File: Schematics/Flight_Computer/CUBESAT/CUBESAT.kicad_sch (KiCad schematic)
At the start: 44 parts, among them J1 6 Pin Connector, J2 M22-6003005, J3 U.FL-R-SMT_01_, U1 ADXL345BCCZ, U2 NEO-M8N-0, U3 IAM-20380, U4 MAGNETOMETER, U5 STM32F446RET6, U6 LM75AIM_NOPB

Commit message: feat: cleaned up schematic for FC
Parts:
- removed J1: 6 Pin Connector, CUBESAT:6 Pin Connector, symbol CUBESAT:6 Pin Connector
- removed R10, R9: 4.7k, CUBESAT:Resistor4.7kO, symbol CUBESAT:Resistor4.7kO
- removed R7: 100, CUBESAT:Reistor100O, symbol CUBESAT:Resistor100O
- added J1: Conn_01x06_Pin, CUBESAT:6 Pin Connector, symbol Connector:Conn_01x06_Pin
- added R11: 100, CUBESAT:Reistor100O, symbol Device:R
- added R13, R7: 4.7k, CUBESAT:Resistor4.7kO, symbol Device:R
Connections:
- net 3.3 V: now also J1.5 (Pin_5), J1.6 (Pin_6), R13.1, R7.1; no longer S2.4
- net I2C 3 SCL: now also R7.2
- net I2C 3 SDA: now also R13.2
- net NRST: now also J1.4 (Pin_4), R11.2
- net SWCLK: now also J1.2 (Pin_2)
- net SWDIO: now also J1.3 (Pin_3)
- net SWO: now also J1.1 (Pin_1)
- net at S1.1: now also R11.1
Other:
- moved on the sheet: C11, R8

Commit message: feat: new updated sch for better readibility
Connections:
- net 3.3 V: now also C14.1, C15.1, C16.1, C17.1, C8.1, R5.1; no longer C1.2, C10.1, C12.2, C13.2, C14.2, C15.2, C16.2, C17.2, C18.2, C19.2, C2.1, C21.2, C3.1, C4.1, C5.1, C6.2, C7.2, C8.2, C9.2, J1.6 (Pin_6), J2.2, J3.1 (GND), J3.2 (GND), R1.1, R4.2, R5.2, R6.2, R8.1, S1.2, S1.4, U1.2 (GND), U1.4 (GND), U1.5 (GND), U2.10 (GND), U2.12 (GND), U2.13 (GND), U2.24 (GND), U2.7 (VDD_USB), U3.10 (RESV9_1215), U3.11 (RESV9_1215), U3.12 (RESV9_1215), U3.13 (GND), U3.15 (RESV9_1215), U3.7 (RESV7), U3.9 (RESV9_1215), U4.3 (GND), U5.12 (VSSA/VREF-), U5.18 (VSS), U5.31 (VSS), U5.47 (VSS), U5.63 (VSS), U6.4 (GND), U6.5 (A2), U6.6 (A1)
- net BOOT0: now also C21.2; no longer C21.1
- net at U6.7 (A0): now also R5.2; no longer R5.1
- net at U5.30 (VCAP_1): now also C18.2; no longer C18.1
- new net GND: C1.2, C10.1, C12.2, C13.2, C14.2, C15.2, C16.2, C17.2, C18.1, C19.2, C2.1, C21.1, C3.1, C4.1, C5.1, C6.2, C7.2, C8.2, C9.2, J1.6 (Pin_6), J2.2, J3.1 (GND), J3.2 (GND), R1.1, R4.2, R6.2, R8.1, S1.2, S1.4, U1.2 (GND), U1.4 (GND), U1.5 (GND), U2.10 (GND), U2.12 (GND), U2.13 (GND), U2.24 (GND), U2.7 (VDD_USB), U3.10 (RESV9_1215), U3.11 (RESV9_1215), U3.12 (RESV9_1215), U3.13 (GND), U3.15 (RESV9_1215), U3.7 (RESV7), U3.9 (RESV9_1215), U4.3 (GND), U5.12 (VSSA/VREF-), U5.18 (VSS), U5.31 (VSS), U5.47 (VSS), U5.63 (VSS), U6.4 (GND), U6.5 (A2), U6.6 (A1)
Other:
- moved on the sheet: C11, C18, C2, C21, C3, C4, C5, R5, R8

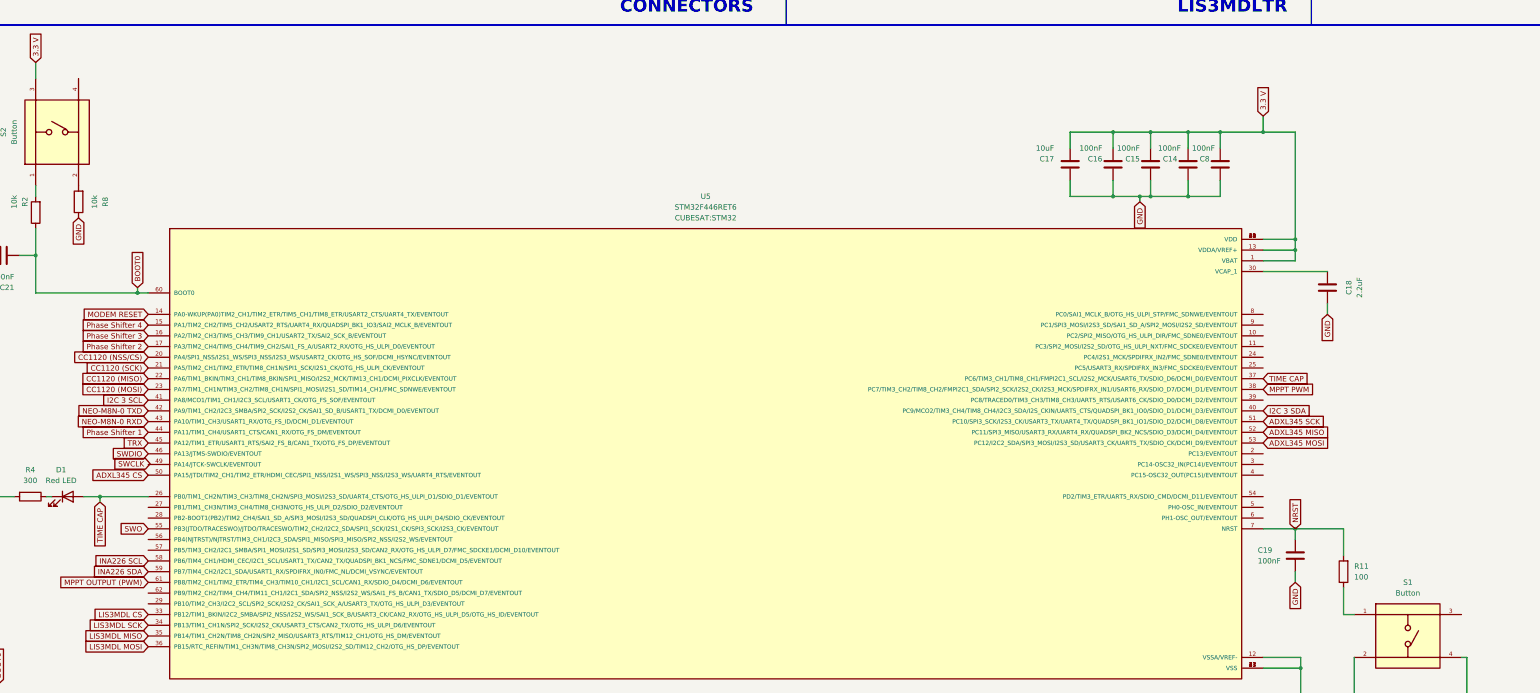
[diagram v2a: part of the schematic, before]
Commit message: feat: add CC1120 drivers
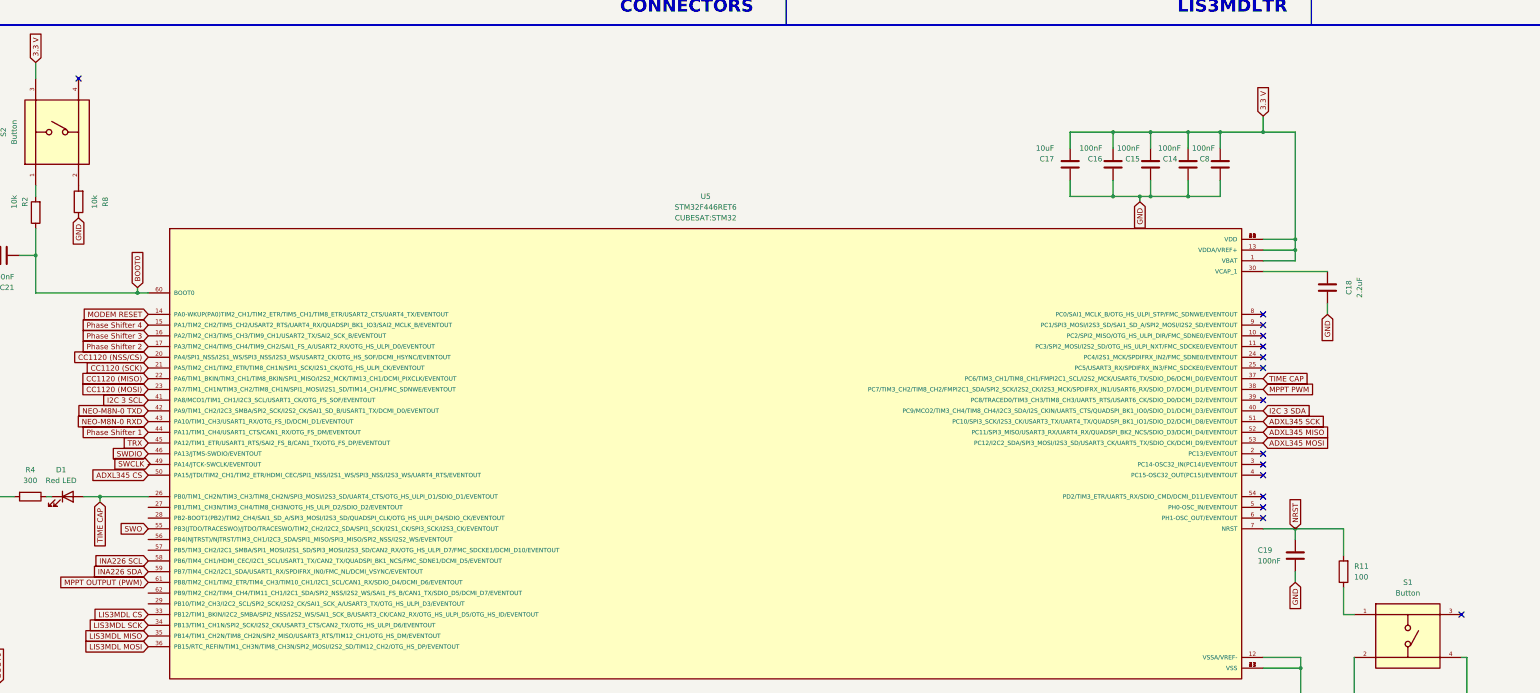
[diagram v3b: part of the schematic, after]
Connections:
- no-connect marks 22 -> 37
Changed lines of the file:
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@@
   )
   (no_connect (at 90.17 167.64))
+  (no_connect (at 483.87 213.36))
   (no_connect (at 44.45 167.64))
   (no_connect (at 109.22 261.62))
+  (no_connect (at 483.87 208.28))
   (no_connect (at 90.17 193.04))
   (no_connect (at 90.17 182.88))
   (no_connect (at 90.17 190.5))
+  (no_connect (at 483.87 220.98))
   (no_connect (at 552.45 63.5))
+  (no_connect (at 483.87 175.26))
+  (no_connect (at 483.87 182.88))
   (no_connect (at 444.5 71.12))
   (no_connect (at 69.85 82.55))
   (no_connect (at 444.5 55.88))
   (no_connect (at 58.42 269.24))
+  (no_connect (at 483.87 177.8))
+  (no_connect (at 483.87 187.96))
   (no_connect (at 44.45 187.96))
   (no_connect (at 44.45 190.5))
   (no_connect (at 444.5 73.66))
   (no_connect (at 90.17 185.42))
+  (no_connect (at 530.86 246.38))
   (no_connect (at 44.45 170.18))
   (no_connect (at 105.41 92.71))
+  (no_connect (at 483.87 195.58))
   (no_connect (at 444.5 58.42))
   (no_connect (at 105.41 82.55))
   (no_connect (at 109.22 264.16))
   (no_connect (at 58.42 271.78))
+  (no_connect (at 203.2 119.38))
+  (no_connect (at 483.87 223.52))
+  (no_connect (at 483.87 218.44))
+  (no_connect (at 483.87 210.82))
+  (no_connect (at 483.87 180.34))
+  (no_connect (at 483.87 185.42))
   (no_connect (at 90.17 170.18))
   (polyline (pts (xy 17.78 229.87) (xy 17.78 299.72))

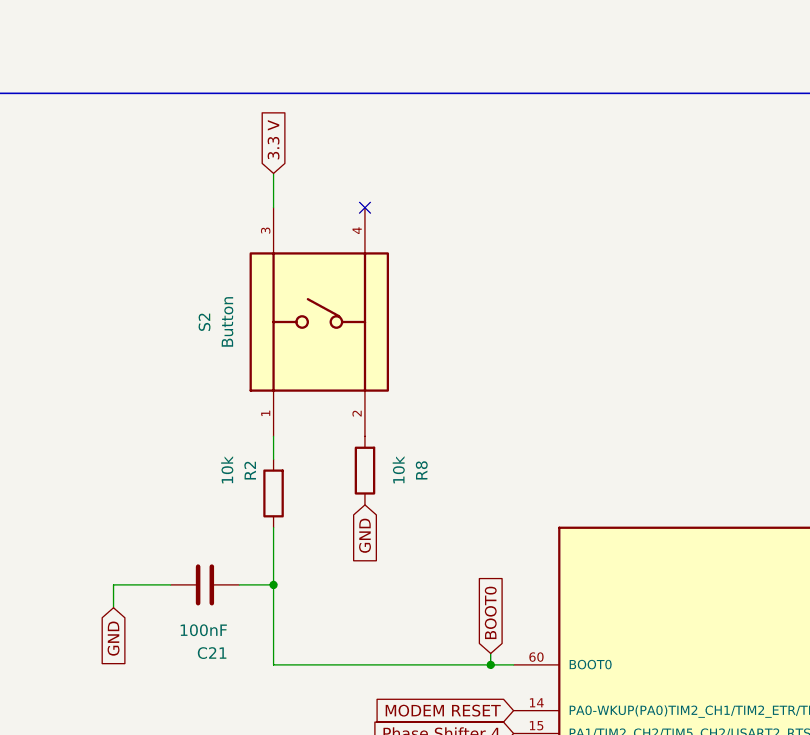
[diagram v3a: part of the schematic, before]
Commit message: fix: add cc1120 bug fixes
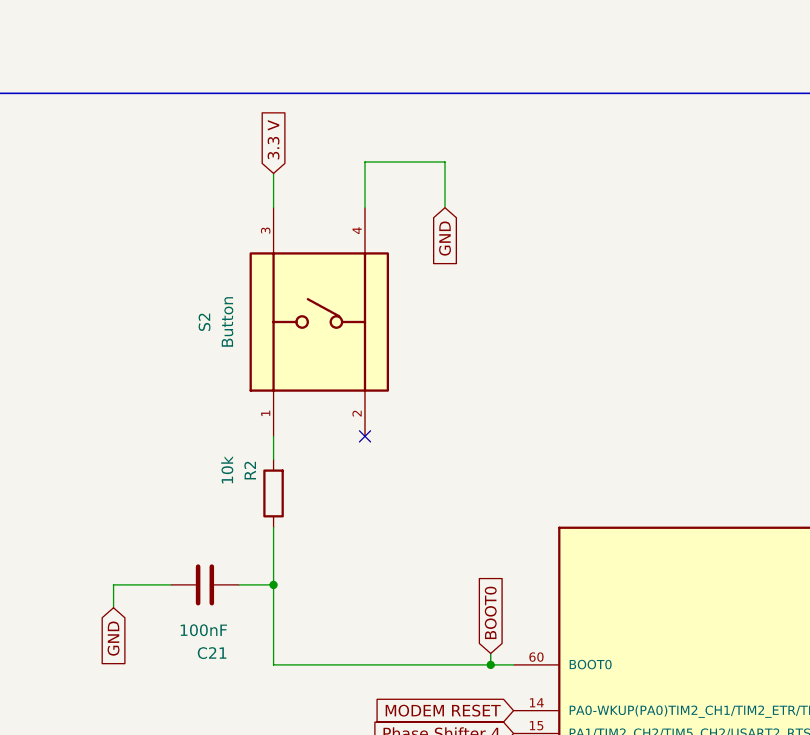
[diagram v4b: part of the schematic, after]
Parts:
- removed R8: 10k, CUBESAT:Resistor10kO, symbol Device:R
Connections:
- net GND: now also S2.4
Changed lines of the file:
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@@
   (no_connect (at 109.22 264.16))
   (no_connect (at 58.42 271.78))
-  (no_connect (at 203.2 119.38))
   (no_connect (at 483.87 223.52))
   (no_connect (at 483.87 218.44))
+  (no_connect (at 203.2 144.78))
   (no_connect (at 483.87 210.82))
   (no_connect (at 483.87 180.34))
@@
     (stroke (width 0) (type default))
   )
+  (wire (pts (xy 212.09 114.3) (xy 212.09 119.38))
+    (stroke (width 0) (type default))
+  )
   (wire (pts (xy 172.72 261.62) (xy 172.72 262.89))
     (stroke (width 0) (type default))
@@
     (stroke (width 0) (type default))
   )
+  (wire (pts (xy 203.2 119.38) (xy 203.2 114.3))
+    (stroke (width 0) (type default))
+  )
   (wire (pts (xy 40.64 95.25) (xy 59.69 95.25))
     (stroke (width 0) (type default))
@@
   )
   (wire (pts (xy 473.71 143.51) (xy 473.71 147.32))
+    (stroke (width 0) (type default))
+  )
+  (wire (pts (xy 203.2 114.3) (xy 212.09 114.3))
     (stroke (width 0) (type default))
   )
@@
     )
   )
-  (global_label "GND" (shape input) (at 203.2 152.4 270) (fields_autoplaced)
-    (effects (font (size 1.27 1.27)) (justify right))
-    (property "Intersheetrefs" "${INTERSHEET_REFS}" (at 203.2 159.2557 90)
-      (effects (font (size 1.27 1.27)) (justify right) hide)
-    )
-  )
   (global_label "I2C 3 SCL" (shape input) (at 219.71 195.58 180) (fields_autoplaced)
     (effects (font (size 1.27 1.27)) (justify right))
@@
     (property "Intersheetrefs" "${INTERSHEET_REFS}" (at 144.7829 87.63 0)
       (effects (font (size 1.27 1.27)) (justify left) hide)
+    )
+  )
+  (global_label "GND" (shape input) (at 212.09 119.38 270) (fields_autoplaced)
+    (effects (font (size 1.27 1.27)) (justify right))
+    (property "Intersheetrefs" "${INTERSHEET_REFS}" (at 212.09 126.2357 90)
+      (effects (font (size 1.27 1.27)) (justify right) hide)
     )
   )
@@
         )
       )
-    )
-  )
-  (symbol (lib_id "Device:R") (at 203.2 148.59 180) (unit 1)
-    (in_bom yes) (on_board yes) (dnp no) (fields_autoplaced)
-    (property "Reference" "R8" (at 209.55 148.59 90)
-      (effects (font (size 1.27 1.27)))
-    )
-    (property "Value" "10k" (at 207.01 148.59 90)
-      (effects (font (size 1.27 1.27)))
-    )
-    (property "Footprint" "CUBESAT:Resistor10kO" (at 199.39 148.59 90)
-      (effects (font (size 1.27 1.27)) hide)
-    )
-    (property "Datasheet" "~" (at 203.2 148.59 0)
-      (effects (font (size 1.27 1.27)) hide)
-    )
-    (pin "1")
-    (pin "2")
-    (instances
-      (project "CUBESAT"
-        (path "/90463ba2-1e71-46b4-87fa-acb95afa2b4b"
-          (reference "R8") (unit 1)
-        )
-      )
